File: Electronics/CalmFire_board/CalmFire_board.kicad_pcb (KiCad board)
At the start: 2 copper layers, 17 parts, among them J1 HT1621_LCD, Q1 IRF8301M, SW1 Rotary_Encoder_Switch, U1 ESP32-DEVKITC-32D, U2 DS18B20, U3 N4100_relay, U4 DHT11

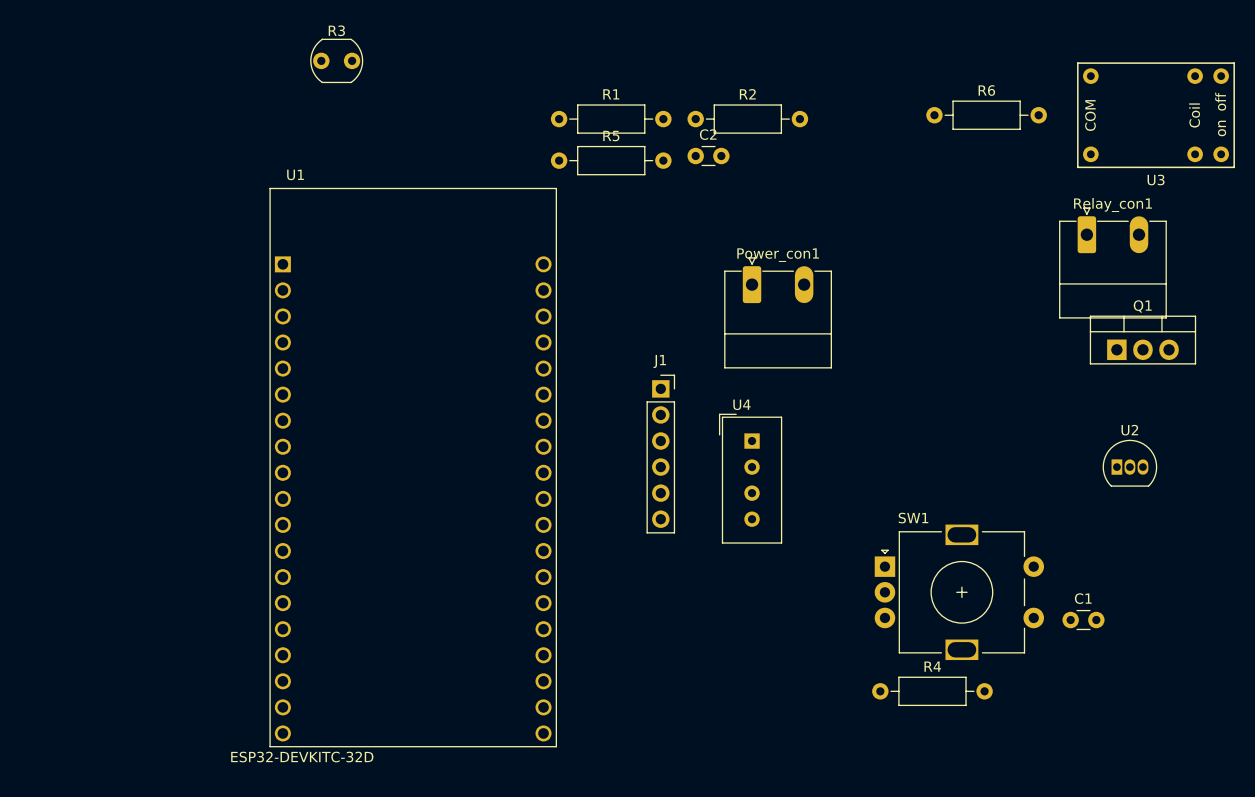
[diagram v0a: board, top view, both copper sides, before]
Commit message: Created ht1621 display footprint. Added power capacitors, power polarity protection N-MOS. Changed temp sensors power to 3.3V and a pull-up on onewire.
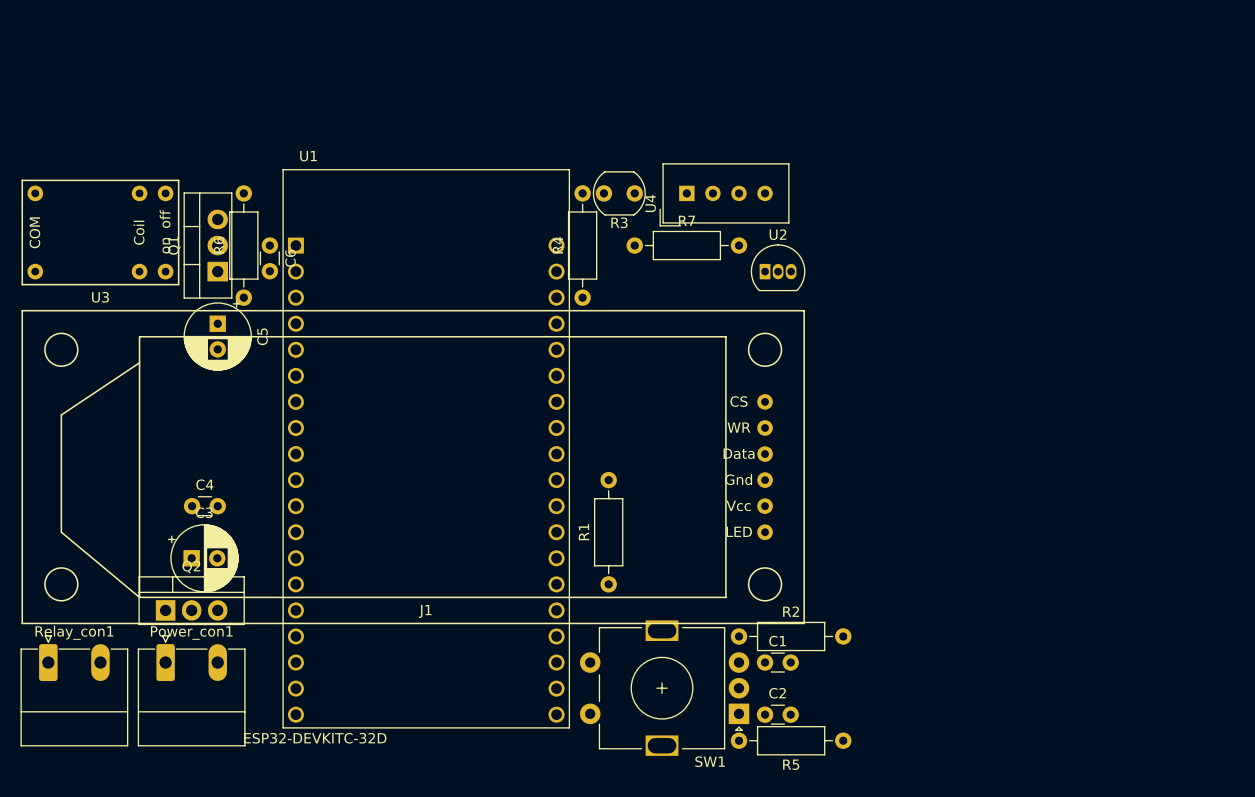
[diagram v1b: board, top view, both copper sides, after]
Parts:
- added C3: 100uF, Capacitor_THT:CP_Radial_D6.3mm_P2.50mm, F.Cu at (-43.2, -25.4)
- added C4: 100nF, Capacitor_THT:C_Disc_D3.0mm_W1.6mm_P2.50mm, F.Cu at (-43.1, -30.5)
- added C5: 100uF, Capacitor_THT:CP_Radial_D6.3mm_P2.50mm, F.Cu at (-40.6, -48.3)
- added C6: 100nF, Capacitor_THT:C_Disc_D3.0mm_W1.6mm_P2.50mm, F.Cu at (-35.6, -55.9)
- added Q2: IRF8301M, Package_TO_SOT_THT:TO-220-3_Vertical, F.Cu at (-45.7, -20.3)
- added R7: 4k7, Resistor_THT:R_Axial_DIN0207_L6.3mm_D2.5mm_P10.16mm_Horizontal, F.Cu at (0.00, -55.9)
- C1, C2: value C_Small -> 220nF
- J1: footprint Connector_PinSocket_2.54mm:PinSocket_1x06_P2.54mm_Vertical -> CalmFire_board:ht1621
- R1, R2, R4, R5: value R_Small -> 10k
- moved Relay_con1 109.5 mm to (-57.1, -15.2)
- moved U3 103.5 mm to (-58.4, -61.0)
- moved Q1 88.0 mm to (-40.6, -53.3), turned to 90 degrees
- moved R6 69.6 mm to (-38.1, -50.8), turned to 90 degrees
- moved Power_con1 68.0 mm to (-45.7, -15.2)
- moved R5 63.0 mm to (20.3, -7.62), turned to 180 degrees
- moved C2 54.9 mm to (12.7, -10.2)
- moved R2 50.6 mm to (10.2, -17.8)
- moved R4 48.1 mm to (-5.08, -50.8), turned to 90 degrees
- moved R1 45.6 mm to (-2.54, -22.9), turned to 90 degrees
- moved U2 39.2 mm to (12.7, -53.3)
- moved R3 33.2 mm to (0.00, -61.0), turned to 180 degrees
- moved C1 30.1 mm to (12.7, -15.2)
- moved U4 25.0 mm to (5.08, -61.0), turned to 90 degrees
- moved SW1 20.2 mm to (10.2, -10.2), turned to 180 degrees
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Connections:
- Power_con1 pad 2: GND -> Net-(Power_con1-Pad2)
- U2 pad 3: +5V -> +3V3
- U4 pad 1: +5V -> +3V3
